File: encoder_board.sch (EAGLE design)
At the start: 13 parts, among them J1 1X2-3.5MM, J2 1X2-3.5MM, J3 1X2-3.5MM, Q1 BSS138, Q2 BSS138, Q3 BSS138, U1 ATtiny85-MU

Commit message: Add files via upload
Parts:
- U1: value ATtiny85-MU -> ATTINY85-20P; device microbuilder:ATTINY85 -> _hhn_attiny25_45_85:ATTINY85-20P
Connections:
- removed net CHANA: U1.(XTAL2/CLK0/OC1B/ADC2/PCINT4)PB4
- removed net CHANB: U1.(XTAL1/CLKI/OC1B/ADC3/PCINT3)PB3
- removed net NC: U1.(MOSI/DI/SDA/AIN0/OC0A/OC1A/AREF/PCINT0)PB0
- net CLK5V: now also U1.PB3; no longer U1.(SCK/USCK/SCL/ADC1/T0/INT0/PCINT2)PB2
- net DATA5V: now also U1.PB4; no longer U1.(MISO/DO/AIN1/OC0B/OC1A/PCINT1)PB1
- net GND: now also U1.PB0, U1.PB1, U1.PB2
- net INT5V: now also U1.NRES/PB5; no longer U1.(RESET/DW/ADC0/PCINT5)PB5

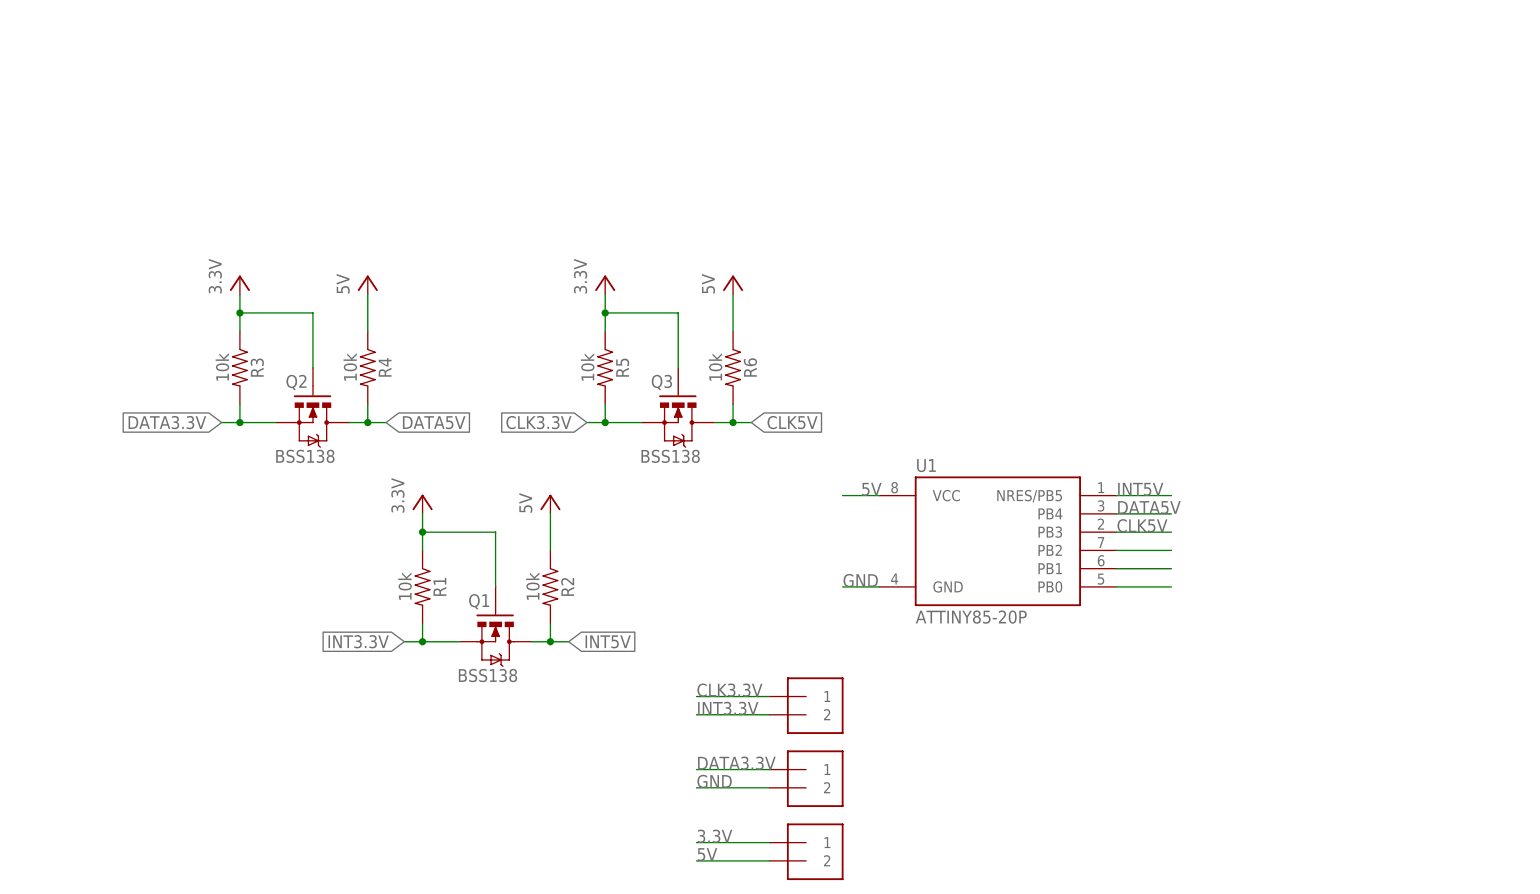
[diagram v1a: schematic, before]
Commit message: updated encoder_board sch
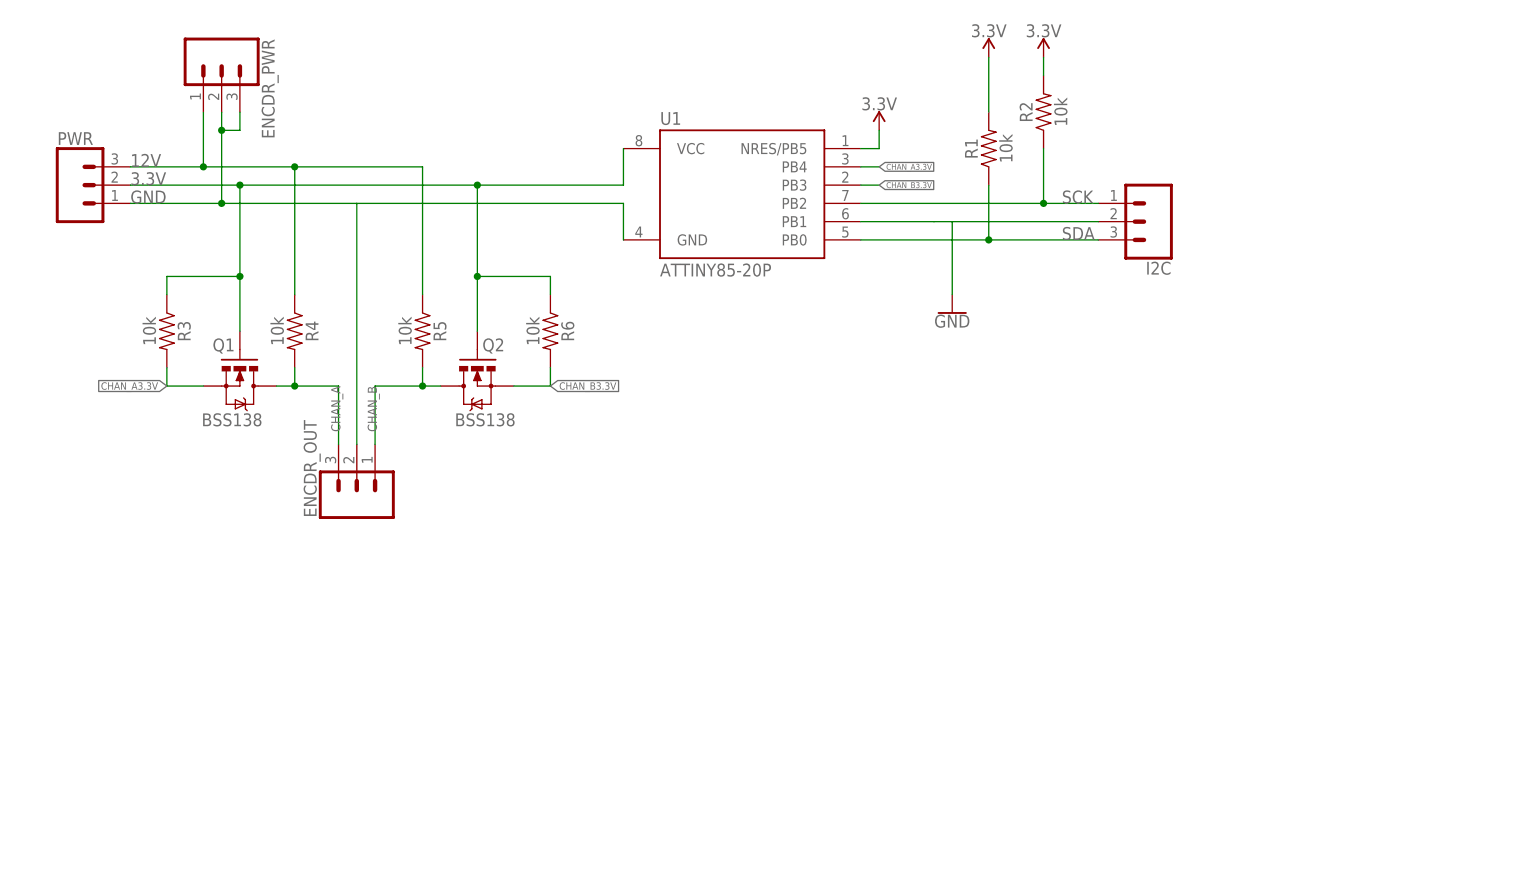
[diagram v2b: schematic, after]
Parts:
- removed J1, J2, J3: 1X2-3.5MM, adafruit:1X2-3.5MM
- removed Q3: BSS138, SparkFun:MOSFET-NCHANNELSMD
- added ENCDR_OUT, ENCDR_PWR, I2C, PWR: (no value), SparkFun-Connectors:CONN_03
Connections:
- removed net 5V: J2.2, R2.1, R4.1, R6.1, U1.VCC
- removed net CLK3.3V: J1.1, Q3.S, R5.2
- removed net CLK5V: Q3.D, R6.2, U1.PB3
- removed net DATA3.3V: J3.1, Q2.S, R3.2
- removed net DATA5V: Q2.D, R4.2, U1.PB4
- removed net INT3.3V: J1.2, Q1.S, R1.2
- removed net INT5V: Q1.D, R2.2, U1.NRES/PB5
- new net 12V: ENCDR_PWR.1, PWR.3, R4.1, R5.1
- new net CHAN_A: ENCDR_OUT.3, Q1.D, R4.2
- new net CHAN_A3.3V: Q1.S, R3.2, U1.PB4
- new net CHAN_B: ENCDR_OUT.1, Q2.D, R5.2
- new net CHAN_B3.3V: Q2.S, R6.2, U1.PB3
- new net SCK: I2C.1, R2.1, U1.PB2
- new net SDA: I2C.3, R1.1, U1.PB0
- net 3.3V: now also PWR.2, R1.2, R2.2, R6.1, U1.NRES/PB5, U1.VCC; no longer J2.1, Q3.G, R1.1, R5.1
- net GND: now also ENCDR_OUT.2, ENCDR_PWR.2, ENCDR_PWR.3, I2C.2, PWR.1; no longer J3.2, U1.PB0, U1.PB2
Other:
- moved on the sheet: Q1, Q2, R1, R2, R3, R4, R5, R6, U1

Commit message: updated headers in encoder_board sch
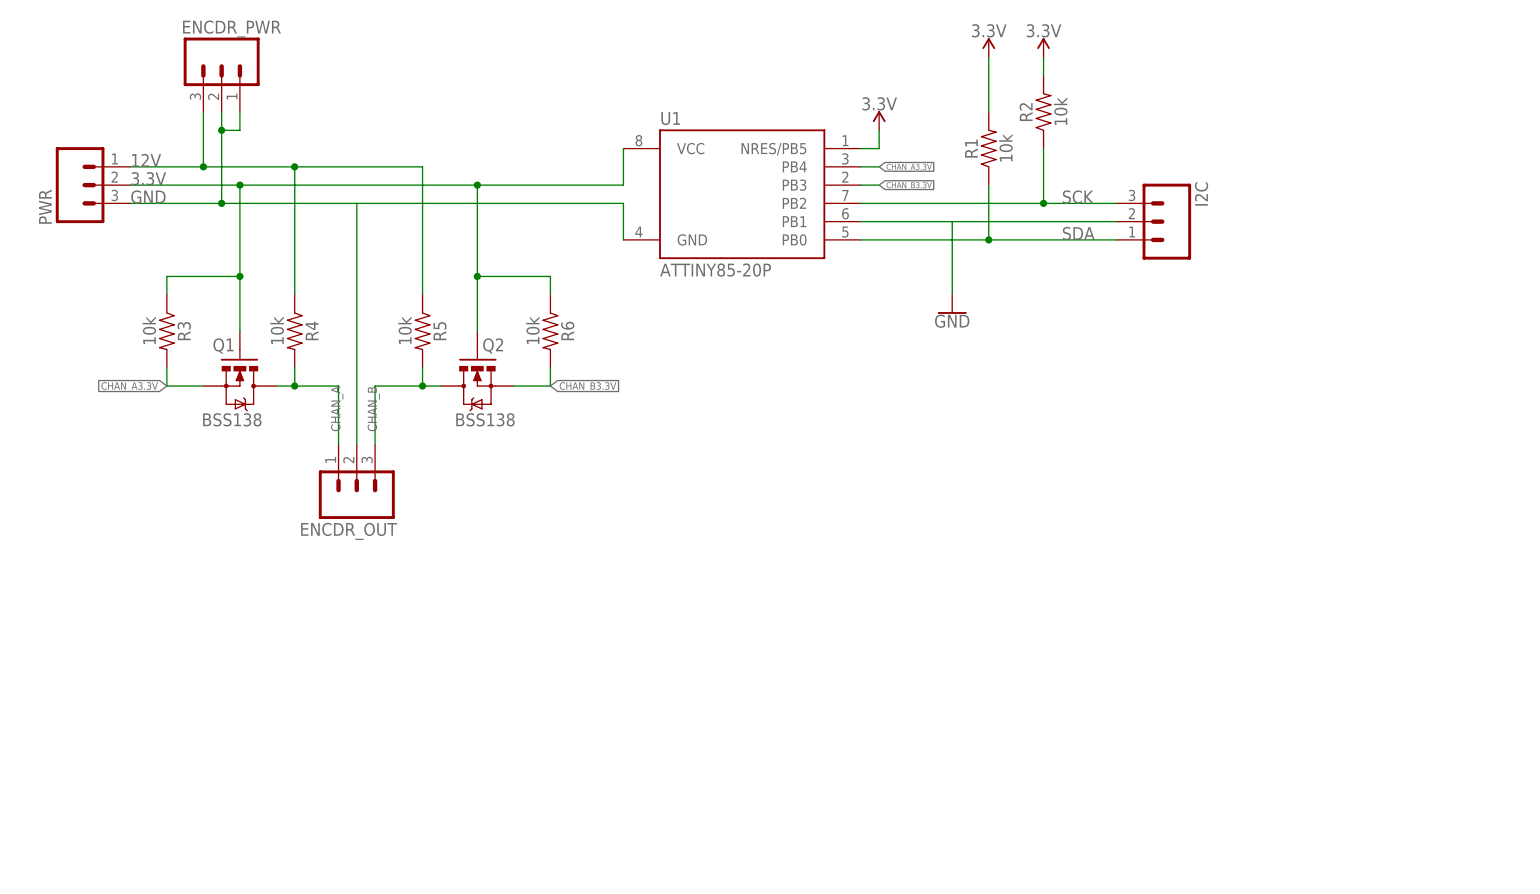
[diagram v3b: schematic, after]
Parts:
- ENCDR_OUT, ENCDR_PWR, I2C, PWR: device SparkFun-Connectors:CONN_03 -> SparkFun-Connectors:CONN_03JST-PTH-VERT
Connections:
- net 12V: now also ENCDR_PWR.3; no longer ENCDR_PWR.1, PWR.3
- net 3.3V: no longer PWR.2
- net CHAN_A: now also ENCDR_OUT.1; no longer ENCDR_OUT.3
- net CHAN_B: now also ENCDR_OUT.3; no longer ENCDR_OUT.1
- net GND: now also ENCDR_PWR.1; no longer ENCDR_PWR.3, PWR.1
- net SCK: now also I2C.3; no longer I2C.1
- net SDA: now also I2C.1; no longer I2C.3
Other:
- moved on the sheet: I2C, PWR
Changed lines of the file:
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@@
 <part name="Q2" library="SparkFun" deviceset="MOSFET-NCHANNEL" device="SMD" value="BSS138"/>
 <part name="U1" library="_hhn_attiny25_45_85" deviceset="ATTINY85*" device="P" technology="-20"/>
-<part name="ENCDR_OUT" library="SparkFun-Connectors" library_urn="urn:adsk.eagle:library:513" deviceset="CONN_03" device="" package3d_urn="urn:adsk.eagle:package:38063/1"/>
-<part name="ENCDR_PWR" library="SparkFun-Connectors" library_urn="urn:adsk.eagle:library:513" deviceset="CONN_03" device="" package3d_urn="urn:adsk.eagle:package:38063/1"/>
-<part name="PWR" library="SparkFun-Connectors" library_urn="urn:adsk.eagle:library:513" deviceset="CONN_03" device="" package3d_urn="urn:adsk.eagle:package:38063/1"/>
-<part name="I2C" library="SparkFun-Connectors" library_urn="urn:adsk.eagle:library:513" deviceset="CONN_03" device="" package3d_urn="urn:adsk.eagle:package:38063/1"/>
 <part name="R1" library="SparkFun-Resistors" library_urn="urn:adsk.eagle:library:532" deviceset="10KOHM" device="-HORIZ-1/4W-1%" package3d_urn="urn:adsk.eagle:package:39658/1" value="10k"/>
 <part name="R2" library="SparkFun-Resistors" library_urn="urn:adsk.eagle:library:532" deviceset="10KOHM" device="-HORIZ-1/4W-1%" package3d_urn="urn:adsk.eagle:package:39658/1" value="10k"/>
@@
 <part name="SUPPLY3" library="SparkFun-PowerSymbols" library_urn="urn:adsk.eagle:library:530" deviceset="VCC" device="" value="3.3V"/>
 <part name="GND1" library="SparkFun-PowerSymbols" library_urn="urn:adsk.eagle:library:530" deviceset="GND" device=""/>
+<part name="I2C" library="SparkFun-Connectors" library_urn="urn:adsk.eagle:library:513" deviceset="CONN_03" device="JST-PTH-VERT" package3d_urn="urn:adsk.eagle:package:38080/1"/>
+<part name="ENCDR_OUT" library="SparkFun-Connectors" library_urn="urn:adsk.eagle:library:513" deviceset="CONN_03" device="JST-PTH-VERT" package3d_urn="urn:adsk.eagle:package:38080/1"/>
+<part name="ENCDR_PWR" library="SparkFun-Connectors" library_urn="urn:adsk.eagle:library:513" deviceset="CONN_03" device="JST-PTH-VERT" package3d_urn="urn:adsk.eagle:package:38080/1"/>
+<part name="PWR" library="SparkFun-Connectors" library_urn="urn:adsk.eagle:library:513" deviceset="CONN_03" device="JST-PTH-VERT" package3d_urn="urn:adsk.eagle:package:38080/1"/>
 </parts>
 <sheets>
@@
 </instance>
 <instance part="U1" gate="G$1" x="119.38" y="86.36"/>
-<instance part="ENCDR_OUT" gate="J$1" x="67.056" y="42.672" rot="R90"/>
-<instance part="ENCDR_PWR" gate="J$1" x="48.26" y="104.14" rot="R270"/>
-<instance part="PWR" gate="J$1" x="27.94" y="86.36"/>
-<instance part="I2C" gate="J$1" x="177.8" y="81.28" rot="R180"/>
 <instance part="R1" gate="G$1" x="154.94" y="91.44" rot="R90"/>
 <instance part="R2" gate="G$1" x="162.56" y="96.52" rot="R90"/>
@@
 <instance part="SUPPLY3" gate="G$1" x="139.7" y="93.98"/>
 <instance part="GND1" gate="1" x="149.86" y="68.58"/>
+<instance part="I2C" gate="J$1" x="180.34" y="81.28" smashed="yes" rot="MR0">
+<attribute name="VALUE" x="182.88" y="73.914" size="1.778" layer="96" font="vector" rot="MR0"/>
+<attribute name="NAME" x="185.42" y="86.868" size="1.778" layer="95" font="vector" rot="MR270"/>
+</instance>
+<instance part="ENCDR_OUT" gate="J$1" x="67.056" y="42.672" smashed="yes" rot="MR90">
+<attribute name="VALUE" x="59.69" y="40.132" size="1.778" layer="96" font="vector" rot="MR90"/>
+<attribute name="NAME" x="72.644" y="37.592" size="1.778" layer="95" font="vector" rot="MR0"/>
+</instance>
+<instance part="ENCDR_PWR" gate="J$1" x="48.26" y="104.14" smashed="yes" rot="MR270">
+<attribute name="VALUE" x="55.626" y="106.68" size="1.778" layer="96" font="vector" rot="MR270"/>
+<attribute name="NAME" x="42.672" y="109.22" size="1.778" layer="95" font="vector" rot="MR180"/>
+</instance>
+<instance part="PWR" gate="J$1" x="27.94" y="86.36" smashed="yes" rot="MR180">
+<attribute name="VALUE" x="25.4" y="93.726" size="1.778" layer="96" font="vector" rot="MR180"/>
+<attribute name="NAME" x="22.86" y="80.772" size="1.778" layer="95" font="vector" rot="MR90"/>
+</instance>
 </instances>
 <busses>
@@
 <wire x1="55.88" y1="58.42" x2="58.42" y2="58.42" width="0.1524" layer="91"/>
 <wire x1="58.42" y1="58.42" x2="58.42" y2="60.96" width="0.1524" layer="91"/>
-<pinref part="ENCDR_OUT" gate="J$1" pin="3"/>
 <wire x1="58.42" y1="58.42" x2="64.516" y2="58.42" width="0.1524" layer="91"/>
 <wire x1="64.516" y1="58.42" x2="64.516" y2="50.292" width="0.1524" layer="91"/>
 <junction x="58.42" y="58.42"/>
 <label x="63.5" y="58.42" size="1.27" layer="95" rot="R270"/>
+<pinref part="ENCDR_OUT" gate="J$1" pin="1"/>
 </segment>
 </net>
@@
 <wire x1="76.2" y1="58.42" x2="69.596" y2="58.42" width="0.1524" layer="91"/>
 <junction x="76.2" y="58.42"/>
-<pinref part="ENCDR_OUT" gate="J$1" pin="1"/>
 <wire x1="69.596" y1="58.42" x2="69.596" y2="50.292" width="0.1524" layer="91"/>
 <label x="68.58" y="58.42" size="1.27" layer="95" rot="R270"/>
+<pinref part="ENCDR_OUT" gate="J$1" pin="3"/>
 </segment>
 </net>
 <net name="12V" class="0">
 <segment>
-<pinref part="PWR" gate="J$1" pin="3"/>
 <wire x1="35.56" y1="88.9" x2="45.72" y2="88.9" width="0.1524" layer="91"/>
 <label x="35.56" y="88.9" size="1.778" layer="95"/>
@@
 <pinref part="R5" gate="G$1" pin="1"/>
 <wire x1="76.2" y1="71.12" x2="76.2" y2="88.9" width="0.1524" layer="91"/>
-<pinref part="ENCDR_PWR" gate="J$1" pin="1"/>
 <wire x1="45.72" y1="96.52" x2="45.72" y2="88.9" width="0.1524" layer="91"/>
 <junction x="45.72" y="88.9"/>
+<pinref part="ENCDR_PWR" gate="J$1" pin="3"/>
 </segment>
 </net>
 <net name="3.3V" class="0">
 <segment>
-<pinref part="PWR" gate="J$1" pin="2"/>
 <wire x1="35.56" y1="86.36" x2="50.8" y2="86.36" width="0.1524" layer="91"/>
 <label x="35.56" y="86.36" size="1.778" layer="95"/>
@@
 <net name="GND" class="0">
 <segment>
-<pinref part="PWR" gate="J$1" pin="1"/>
 <wire x1="35.56" y1="83.82" x2="48.26" y2="83.82" width="0.1524" layer="91"/>
 <label x="35.56" y="83.82" size="1.778" layer="95"/>
@@
 <wire x1="67.056" y1="83.82" x2="104.14" y2="83.82" width="0.1524" layer="91"/>
 <wire x1="104.14" y1="83.82" x2="104.14" y2="78.74" width="0.1524" layer="91"/>
-<pinref part="ENCDR_OUT" gate="J$1" pin="2"/>
 <wire x1="67.056" y1="50.292" x2="67.056" y2="83.82" width="0.1524" layer="91"/>
-<pinref part="ENCDR_PWR" gate="J$1" pin="2"/>
 <wire x1="48.26" y1="96.52" x2="48.26" y2="93.98" width="0.1524" layer="91"/>
 <junction x="48.26" y="83.82"/>
@@
 <wire x1="48.26" y1="93.98" x2="50.8" y2="93.98" width="0.1524" layer="91"/>
 <junction x="48.26" y="93.98"/>
-<pinref part="ENCDR_PWR" gate="J$1" pin="3"/>
 <wire x1="50.8" y1="93.98" x2="50.8" y2="96.52" width="0.1524" layer="91"/>
-</segment>
-<segment>
-<pinref part="I2C" gate="J$1" pin="2"/>
+<pinref part="ENCDR_OUT" gate="J$1" pin="2"/>
+<pinref part="ENCDR_PWR" gate="J$1" pin="1"/>
+<pinref part="ENCDR_PWR" gate="J$1" pin="2"/>
+</segment>
+<segment>
 <pinref part="U1" gate="G$1" pin="PB1"/>
-<wire x1="170.18" y1="81.28" x2="149.86" y2="81.28" width="0.1524" layer="91"/>
-<wire x1="147.32" y1="81.28" x2="137.16" y2="81.28" width="0.1524" layer="91"/>
-<wire x1="147.32" y1="81.28" x2="149.86" y2="81.28" width="0.1524" layer="91"/>
+<wire x1="172.72" y1="81.28" x2="149.86" y2="81.28" width="0.1524" layer="91"/>
+<wire x1="149.86" y1="81.28" x2="137.16" y2="81.28" width="0.1524" layer="91"/>
 <wire x1="149.86" y1="81.28" x2="149.86" y2="71.12" width="0.1524" layer="91"/>
 <pinref part="GND1" gate="1" pin="GND"/>
+<pinref part="I2C" gate="J$1" pin="2"/>
 </segment>
 </net>
@@
 <segment>
 <pinref part="U1" gate="G$1" pin="PB0"/>
-<pinref part="I2C" gate="J$1" pin="3"/>
 <wire x1="137.16" y1="78.74" x2="154.94" y2="78.74" width="0.1524" layer="91"/>
 <label x="165.1" y="78.74" size="1.778" layer="95"/>
 <pinref part="R1" gate="G$1" pin="1"/>
-<wire x1="154.94" y1="78.74" x2="170.18" y2="78.74" width="0.1524" layer="91"/>
+<wire x1="154.94" y1="78.74" x2="172.72" y2="78.74" width="0.1524" layer="91"/>
 <wire x1="154.94" y1="86.36" x2="154.94" y2="78.74" width="0.1524" layer="91"/>
 <junction x="154.94" y="78.74"/>
+<pinref part="I2C" gate="J$1" pin="1"/>
 </segment>
 </net>
@@
 <segment>
 <pinref part="U1" gate="G$1" pin="PB2"/>
-<pinref part="I2C" gate="J$1" pin="1"/>
 <wire x1="137.16" y1="83.82" x2="162.56" y2="83.82" width="0.1524" layer="91"/>
 <label x="165.1" y="83.82" size="1.778" layer="95"/>
 <pinref part="R2" gate="G$1" pin="1"/>
-<wire x1="162.56" y1="83.82" x2="170.18" y2="83.82" width="0.1524" layer="91"/>
+<wire x1="162.56" y1="83.82" x2="172.72" y2="83.82" width="0.1524" layer="91"/>
 <wire x1="162.56" y1="91.44" x2="162.56" y2="83.82" width="0.1524" layer="91"/>
 <junction x="162.56" y="83.82"/>
-</segment>
-</net>
+<pinref part="I2C" gate="J$1" pin="3"/>
+</segment>
+</net>

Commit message: Add files via upload
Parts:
- removed ENCDR_OUT, ENCDR_PWR: (no value), SparkFun-Connectors:CONN_03JST-PTH-VERT
- removed R1, R2: 10k, SparkFun-Resistors:10KOHM-HORIZ-1/4W-1%
- added ENCODER: B6B-EH-A, con-jst-eh:B6B-EH-A
- added R7: 10k, SparkFun-Resistors:10KOHM-HORIZ-1/4W-1%
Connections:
- removed net CHAN_A: ENCDR_OUT.1, Q1.D, R4.2
- removed net CHAN_B: ENCDR_OUT.3, Q2.D, R5.2
- new net CHAN_A5V: ENCODER.6, Q1.D, R4.2
- new net CHAN_B5V: ENCODER.5, Q2.D, R5.2
- new net N$1: R7.1, U1.NRES/PB5
- net 12V: now also ENCODER.1, PWR.1; no longer ENCDR_PWR.3
- net 3.3V: now also PWR.2, R7.2; no longer R1.2, R2.2, U1.NRES/PB5
- net GND: now also ENCODER.2, ENCODER.3, ENCODER.4, PWR.3; no longer ENCDR_OUT.2, ENCDR_PWR.1, ENCDR_PWR.2
- net SCK: no longer R2.1
- net SDA: no longer R1.1
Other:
- moved on the sheet: PWR
